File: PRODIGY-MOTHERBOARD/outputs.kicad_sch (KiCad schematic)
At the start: 36 parts, among them J10 MOTOR, J11 CAN, J3 A_IN, J4 SPI_OUT, J5 12V OUT, J6 I2C, J7 Neopixel, J8 USB_A, J9 SERIAL, U3 PCA9306DC

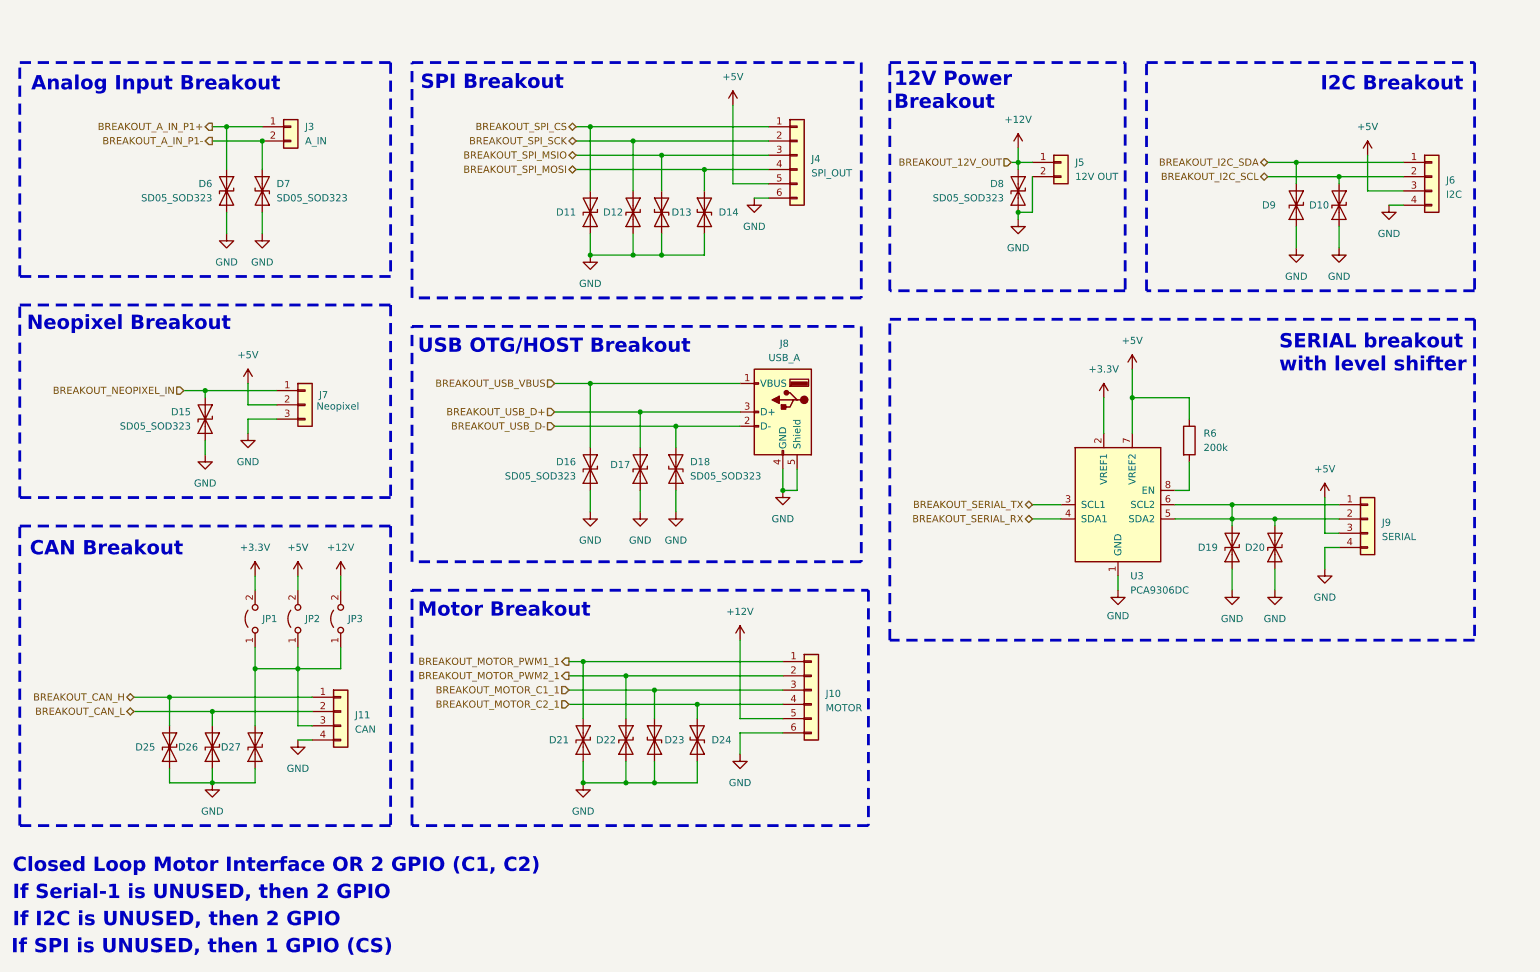
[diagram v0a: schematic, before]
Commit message: MCU schematic done. Started Analog design.
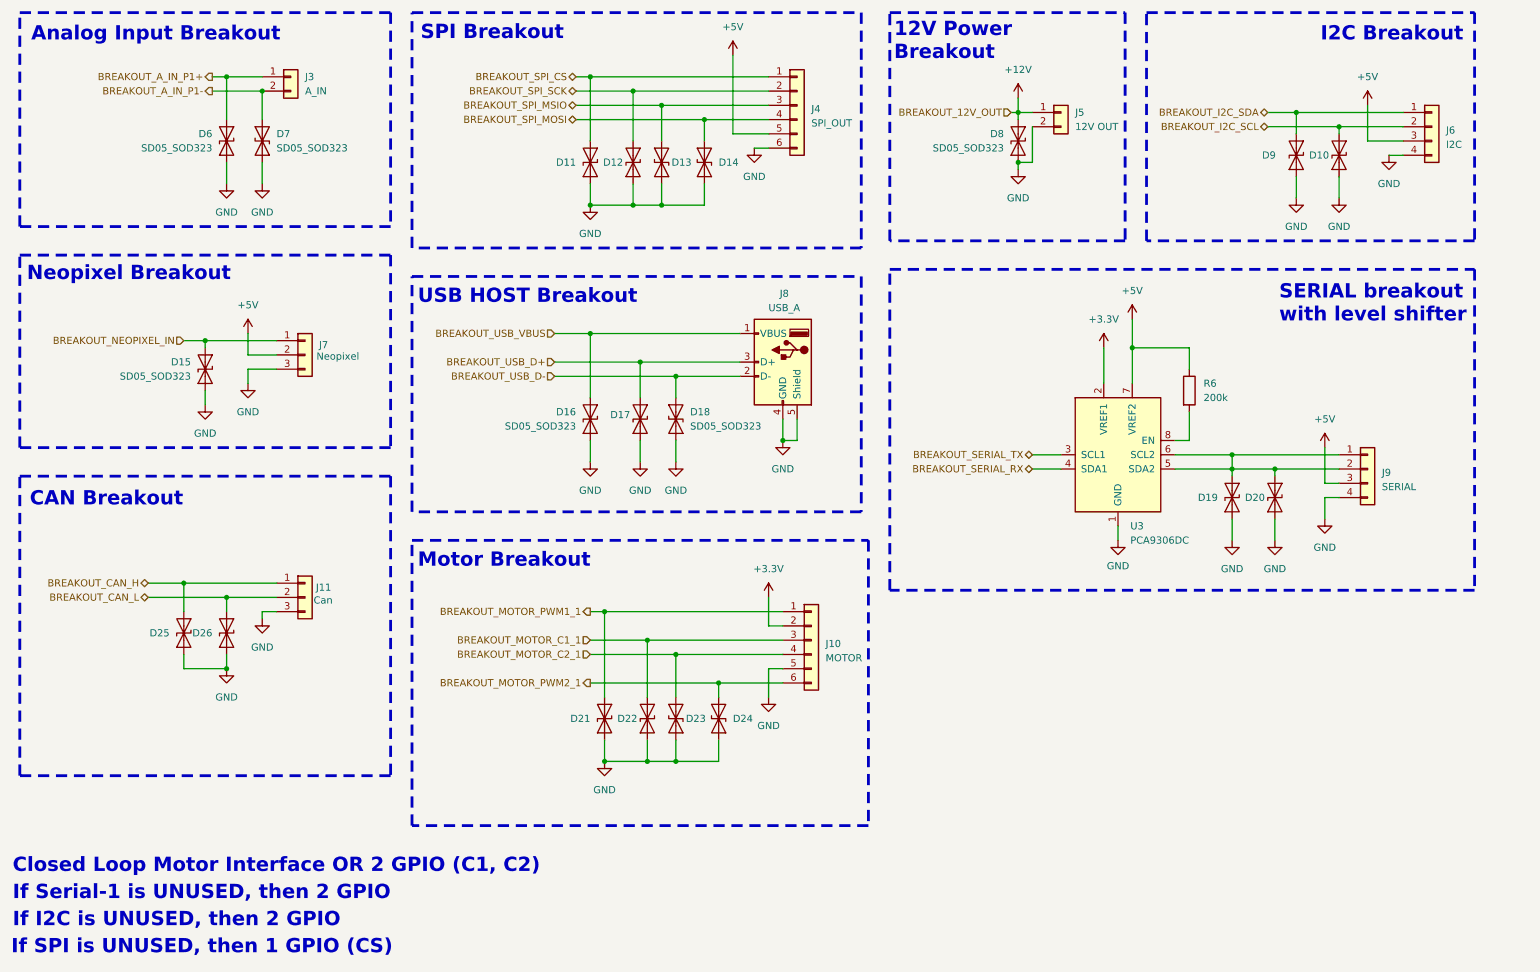
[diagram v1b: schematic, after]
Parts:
- removed D27: SD05_SOD323, Diode_SMD:D_SOD-323, symbol Diode:SD05_SOD323
- removed J11: CAN, Connector_JST:JST_XH_S4B-XH-A_1x04_P2.50mm_Horizontal, symbol Connector_Generic:Conn_01x04
- removed JP1, JP2, JP3: Jumper_2_Open, symbol Jumper:Jumper_2_Open
- added J11: Can, Connector_JST:JST_XH_S3B-XH-A_1x03_P2.50mm_Horizontal, symbol Connector_Generic:Conn_01x03
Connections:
- net +12V: no longer J10.5 (Pin_5)
- net +3.3V: now also J10.2 (Pin_2)
- net BREAKOUT_CAN_H: now also J11.1 (Pin_1)
- net BREAKOUT_CAN_L: now also J11.2 (Pin_2)
- net BREAKOUT_MOTOR_C1_1: now also D22.2 (A2); no longer D23.2 (A2)
- net BREAKOUT_MOTOR_C2_1: now also D23.2 (A2); no longer D24.2 (A2)
- net BREAKOUT_MOTOR_PWM2_1: now also D24.2 (A2), J10.6 (Pin_6); no longer D22.2 (A2), J10.2 (Pin_2)
- net GND: now also J10.5 (Pin_5), J11.3 (Pin_3); no longer J10.6 (Pin_6)
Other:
- note added: "USB HOST Breakout"
- note removed: "USB OTG/HOST Breakout"
- moved on the sheet: D10, D11, D12, D13, D14, D15, D16, D17, D18, D19, D20, D21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

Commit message: Finished v0.1 schematic.
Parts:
- added D30, D32, D33, D34: SD05_SOD323, Diode_SMD:D_SOD-323, symbol Diode:SD05_SOD323
- added J16: RTD_PT100, Connector_Phoenix_MSTB:PhoenixContact_MSTBA_2,5_4-G-5,08_1x04_P5.08mm_Horizontal, symbol Connector_Generic:Conn_01x04
- J10: renamed from J7; footprint Connector_JST:JST_XH_S3B-XH-A_1x03_P2.50mm_Horizontal -> Connector_Phoenix_MSTB:PhoenixContact_MSTBA_2,5_3-G-5,08_1x03_P5.08mm_Horizontal
- J11: footprint Connector_JST:JST_XH_S3B-XH-A_1x03_P2.50mm_Horizontal -> Connector_Phoenix_MSTB:PhoenixContact_MSTBA_2,5_3-G-5,08_1x03_P5.08mm_Horizontal
- J13: renamed from J4; footprint Connector_JST:JST_XH_S6B-XH-A_1x06_P2.50mm_Horizontal -> Connector_Phoenix_MSTB:PhoenixContact_MSTBA_2,5_6-G-5,08_1x06_P5.08mm_Horizontal
- J14: renamed from J10; footprint Connector_JST:JST_XH_S6B-XH-A_1x06_P2.50mm_Horizontal -> Connector_Phoenix_MSTB:PhoenixContact_MSTBA_2,5_6-G-5,08_1x06_P5.08mm_Horizontal
- J15: renamed from J5; footprint TerminalBlock_Phoenix:TerminalBlock_Phoenix_MKDS-1,5-2-5.08_1x02_P5.08mm_Horizontal -> Connector_Phoenix_MSTB:PhoenixContact_MSTBA_2,5_2-G-5,08_1x02_P5.08mm_Horizontal
- J17: renamed from J9; footprint Connector_JST:JST_XH_S4B-XH-A_1x04_P2.50mm_Horizontal -> Connector_Phoenix_MSTB:PhoenixContact_MSTBA_2,5_4-G-5,08_1x04_P5.08mm_Horizontal
- J18: renamed from J6; footprint Connector_JST:JST_XH_S4B-XH-A_1x04_P2.50mm_Horizontal -> Connector_Phoenix_MSTB:PhoenixContact_MSTBA_2,5_4-G-5,08_1x04_P5.08mm_Horizontal
- J9: renamed from J3; footprint Connector_JST:JST_XH_S3B-XH-A_1x02_P2.50mm_Horizontal -> Connector_Phoenix_MSTB:PhoenixContact_MSTBA_2,5_2-G-5,08_1x02_P5.08mm_Horizontal
- renumbered D25 to D14, D6 to D16, D26 to D17, D7 to D18, D11 to D19, D16 to D20, D12 to D22, D17 to D23, D22 to D24, D13 to D25, D18 to D26, D23 to D27, D14 to D28, D24 to D29, D8 to D31, D19 to D35, D20 to D36, D9 to D37, D10 to D38, J8 to J12, R6 to R26, U3 to U6
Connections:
- net GND: now also D30.1 (A1), D32.1 (A1), D33.1 (A1), D34.1 (A1)
- new net RTD_W1: D30.2 (A2), J16.1 (Pin_1)
- new net RTD_W2: D32.2 (A2), J16.2 (Pin_2)
- new net RTD_W3: D33.2 (A2), J16.3 (Pin_3)
- new net RTD_W4: D34.2 (A2), J16.4 (Pin_4)
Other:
- note added: "PT100/PT1000 Breakout"
- note added: "Piezo Sensor Input Breakout"
- note removed: "Analog Input Breakout"
- note removed: "Closed Loop Motor Interface OR 2 GPIO (C1, C2)"
- note removed: "If I2C is UNUSED, then 2 GPIO"
- note removed: "If SPI is UNUSED, then 1 GPIO (CS)"
- note removed: "If Serial-1 is UNUSED, then 2 GPIO"
- moved on the sheet: D14, D15, D17, J10, J11

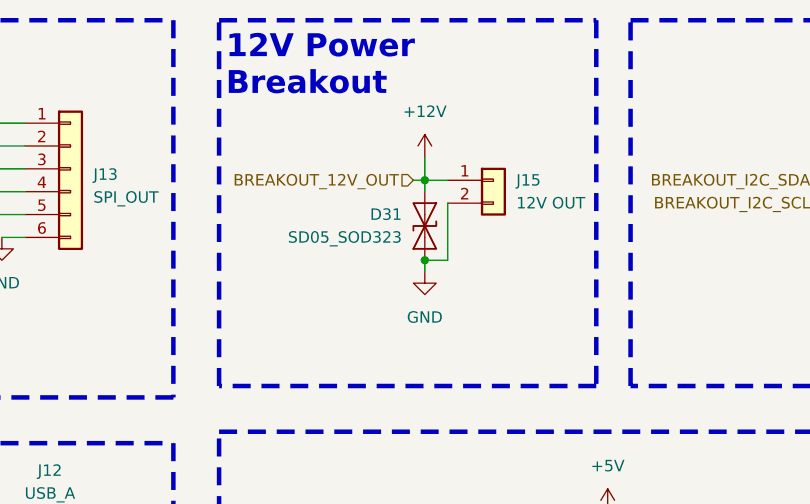
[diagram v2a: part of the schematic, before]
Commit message: MBT Schematic improved
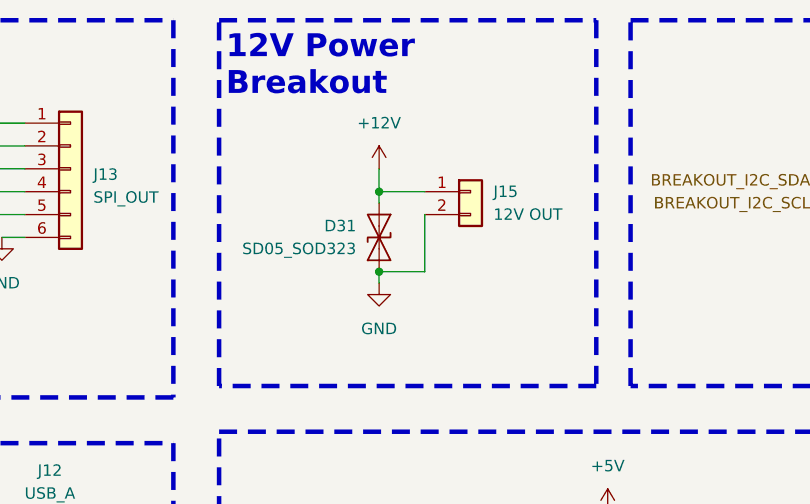
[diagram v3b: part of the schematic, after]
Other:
- moved on the sheet: D31, J15
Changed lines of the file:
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@@
 	(paper "A4")
 	(junction
-		(at 195.58 35.56)
+		(at 190.5 36.83)
 		(diameter 0)
 		(color 0 0 0 0)
@@
 	)
 	(junction
-		(at 195.58 44.45)
+		(at 190.5 45.72)
 		(diameter 0)
 		(color 0 0 0 0)
@@
 	(wire
 		(pts
-			(xy 195.58 33.02) (xy 195.58 35.56)
+			(xy 190.5 34.29) (xy 190.5 36.83)
 		)
 		(stroke
@@
 	(wire
 		(pts
-			(xy 195.58 36.83) (xy 195.58 35.56)
+			(xy 190.5 38.1) (xy 190.5 36.83)
 		)
 		(stroke
@@
 	(wire
 		(pts
-			(xy 195.58 35.56) (xy 198.12 35.56)
+			(xy 190.5 36.83) (xy 195.58 36.83)
 		)
 		(stroke
@@
 	(wire
 		(pts
-			(xy 194.31 35.56) (xy 195.58 35.56)
-		)
-		(stroke
-			(width 0)
-			(type default)
-		)
-	)
-	(wire
-		(pts
 			(xy 257.81 34.29) (xy 257.81 40.64)
 		)
@@
 	(wire
 		(pts
-			(xy 198.12 38.1) (xy 198.12 44.45)
+			(xy 195.58 39.37) (xy 195.58 45.72)
 		)
 		(stroke
@@
 	(wire
 		(pts
-			(xy 195.58 44.45) (xy 195.58 45.72)
+			(xy 190.5 45.72) (xy 190.5 46.99)
 		)
 		(stroke
@@
 	(wire
 		(pts
-			(xy 198.12 44.45) (xy 195.58 44.45)
+			(xy 195.58 45.72) (xy 190.5 45.72)
 		)
 		(stroke
@@
 		)
 	)
-	(hierarchical_label "BREAKOUT_12V_OUT"
-		(shape input)
-		(at 194.31 35.56 180)
-		(fields_autoplaced yes)
-		(effects
-			(font
-				(size 1.27 1.27)
-			)
-			(justify right)
-		)
-	)
 	(hierarchical_label "BREAKOUT_I2C_SDA"
 		(shape bidirectional)
@@
 	(symbol
 		(lib_id "power:GND")
-		(at 195.58 45.72 0)
+		(at 190.5 46.99 0)
 		(unit 1)
 		(exclude_from_sim no)
@@
 		(fields_autoplaced yes)
 		(property "Reference" "#PWR088"
-			(at 195.58 52.07 0)
+			(at 190.5 53.34 0)
 			(effects
 				(font
@@
 		)
 		(property "Value" "GND"
-			(at 195.58 50.8 0)
+			(at 190.5 52.07 0)
 			(effects
 				(font
@@
 		)
 		(property "Footprint" ""
-			(at 195.58 45.72 0)
+			(at 190.5 46.99 0)
 			(effects
 				(font
@@
 		)
 		(property "Datasheet" ""
-			(at 195.58 45.72 0)
+			(at 190.5 46.99 0)
 			(effects
 				(font
@@
 		)
 		(property "Description" ""
-			(at 195.58 45.72 0)
+			(at 190.5 46.99 0)
 			(effects
 				(font
@@
 	(symbol
 		(lib_id "Connector_Generic:Conn_01x02")
-		(at 203.2 35.56 0)
+		(at 200.66 36.83 0)
 		(unit 1)
 		(exclude_from_sim no)
@@
 		(fields_autoplaced yes)
 		(property "Reference" "J15"
-			(at 205.74 35.5599 0)
+			(at 203.2 36.8299 0)
 			(effects
 				(font
@@
 		)
 		(property "Value" "12V OUT "
-			(at 205.74 38.0999 0)
+			(at 203.2 39.3699 0)
 			(effects
 				(font
@@
 		)
 		(property "Footprint" "Connector_Phoenix_MSTB:PhoenixContact_MSTBA_2,5_2-G-5,08_1x02_P5.08mm_Horizontal"
-			(at 203.2 35.56 0)
+			(at 200.66 36.83 0)
 			(effects
 				(font
@@
 		)
 		(property "Datasheet" "~"
-			(at 203.2 35.56 0)
+			(at 200.66 36.83 0)
 			(effects
 				(font
@@
 		)
 		(property "Description" "Generic connector, single row, 01x02, script generated (kicad-library-utils/schlib/autogen/connector/)"
-			(at 203.2 35.56 0)
+			(at 200.66 36.83 0)
 			(effects
 				(font
@@
 	(symbol
 		(lib_id "power:+12V")
-		(at 195.58 33.02 0)
+		(at 190.5 34.29 0)
 		(unit 1)
 		(exclude_from_sim no)
@@
 		(fields_autoplaced yes)
 		(property "Reference" "#PWR087"
-			(at 195.58 36.83 0)
+			(at 190.5 38.1 0)
 			(effects
 				(font
@@
 		)
 		(property "Value" "+12V"
-			(at 195.58 27.94 0)
+			(at 190.5 29.21 0)
 			(effects
 				(font
@@
 		)
 		(property "Footprint" ""
-			(at 195.58 33.02 0)
+			(at 190.5 34.29 0)
 			(effects
 				(font
@@
 		)
 		(property "Datasheet" ""
-			(at 195.58 33.02 0)
+			(at 190.5 34.29 0)
 			(effects
 				(font
@@
 		)
 		(property "Description" "Power symbol creates a global label with name \"+12V\""
-			(at 195.58 33.02 0)
+			(at 190.5 34.29 0)
 			(effects
 				(font
@@
 	(symbol
 		(lib_id "Diode:SD05_SOD323")
-		(at 195.58 40.64 270)
+		(at 190.5 41.91 270)
 		(mirror x)
 		(unit 1)
@@
 		(dnp no)
 		(property "Reference" "D31"
-			(at 193.04 39.3699 90)
+			(at 187.96 40.6399 90)
 			(effects
 				(font
@@
 		)
 		(property "Value" "SD05_SOD323"
-			(at 193.04 41.9099 90)
+			(at 187.96 43.1799 90)
 			(effects
 				(font
@@
 		)
 		(property "Footprint" "Diode_SMD:D_SOD-323"
-			(at 190.5 40.64 0)
+			(at 185.42 41.91 0)
 			(effects
 				(font
@@
 		)
 		(property "Datasheet" "https://www.littelfuse.com/~/media/electronics/datasheets/tvs_diode_arrays/littelfuse_tvs_diode_array_sd_c_datasheet.pdf.pdf"
-			(at 195.58 40.64 0)
+			(at 190.5 41.91 0)
 			(effects
 				(font
@@
 		)
 		(property "Description" "5V, 450W Discrete Bidirectional TVS Diode, SOD-323"
-			(at 195.58 40.64 0)
+			(at 190.5 41.91 0)
 			(effects
 				(font

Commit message: schematic v0.2 finalized
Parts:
- renumbered D30 to D14, D32 to D15, D14 to D16, D33 to D17, D16 to D18, D17 to D19, D34 to D20, D18 to D21, D19 to D22, D20 to D23, D21 to D24, D22 to D25, D23 to D26, D24 to D27, D25 to D28, D26 to D29, D27 to D30, D28 to D31, D29 to D32, D31 to D33, D15 to D34, J16 to J10, J10 to J16

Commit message: changed breakout connectors and bpc size
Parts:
- J10, J17, J18: footprint Connector_Phoenix_MSTB:PhoenixContact_MSTBA_2,5_4-G-5,08_1x04_P5.08mm_Horizontal -> TerminalBlock_Phoenix:TerminalBlock_Phoenix_MKDS-1,5-4-5.08_1x04_P5.08mm_Horizontal
- J11, J16: footprint Connector_Phoenix_MSTB:PhoenixContact_MSTBA_2,5_3-G-5,08_1x03_P5.08mm_Horizontal -> TerminalBlock_Phoenix:TerminalBlock_Phoenix_MKDS-1,5-3-5.08_1x03_P5.08mm_Horizontal
- J13, J14: footprint Connector_Phoenix_MSTB:PhoenixContact_MSTBA_2,5_6-G-5,08_1x06_P5.08mm_Horizontal -> TerminalBlock_Phoenix:TerminalBlock_Phoenix_MKDS-1,5-6-5.08_1x06_P5.08mm_Horizontal
- J15, J9: footprint Connector_Phoenix_MSTB:PhoenixContact_MSTBA_2,5_2-G-5,08_1x02_P5.08mm_Horizontal -> TerminalBlock_Phoenix:TerminalBlock_Phoenix_MKDS-1,5-2-5.08_1x02_P5.08mm_Horizontal
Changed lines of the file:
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@@
 			)
 		)
-		(property "Footprint" "Connector_Phoenix_MSTB:PhoenixContact_MSTBA_2,5_6-G-5,08_1x06_P5.08mm_Horizontal"
+		(property "Footprint" "TerminalBlock_Phoenix:TerminalBlock_Phoenix_MKDS-1,5-6-5.08_1x06_P5.08mm_Horizontal"
 			(at 158.75 129.54 0)
 			(effects
@@
 			)
 		)
-		(property "Footprint" "Connector_Phoenix_MSTB:PhoenixContact_MSTBA_2,5_4-G-5,08_1x04_P5.08mm_Horizontal"
+		(property "Footprint" "TerminalBlock_Phoenix:TerminalBlock_Phoenix_MKDS-1,5-4-5.08_1x04_P5.08mm_Horizontal"
 			(at 269.24 38.1 0)
 			(effects
@@
 			)
 		)
-		(property "Footprint" "Connector_Phoenix_MSTB:PhoenixContact_MSTBA_2,5_4-G-5,08_1x04_P5.08mm_Horizontal"
+		(property "Footprint" "TerminalBlock_Phoenix:TerminalBlock_Phoenix_MKDS-1,5-4-5.08_1x04_P5.08mm_Horizontal"
 			(at 67.31 71.12 0)
 			(effects
@@
 			)
 		)
-		(property "Footprint" "Connector_Phoenix_MSTB:PhoenixContact_MSTBA_2,5_2-G-5,08_1x02_P5.08mm_Horizontal"
+		(property "Footprint" "TerminalBlock_Phoenix:TerminalBlock_Phoenix_MKDS-1,5-2-5.08_1x02_P5.08mm_Horizontal"
 			(at 200.66 36.83 0)
 			(effects
@@
 			)
 		)
-		(property "Footprint" "Connector_Phoenix_MSTB:PhoenixContact_MSTBA_2,5_3-G-5,08_1x03_P5.08mm_Horizontal"
+		(property "Footprint" "TerminalBlock_Phoenix:TerminalBlock_Phoenix_MKDS-1,5-3-5.08_1x03_P5.08mm_Horizontal"
 			(at 71.12 123.19 0)
 			(effects
@@
 			)
 		)
-		(property "Footprint" "Connector_Phoenix_MSTB:PhoenixContact_MSTBA_2,5_2-G-5,08_1x02_P5.08mm_Horizontal"
+		(property "Footprint" "TerminalBlock_Phoenix:TerminalBlock_Phoenix_MKDS-1,5-2-5.08_1x02_P5.08mm_Horizontal"
 			(at 66.04 29.21 0)
 			(effects
@@
 			)
 		)
-		(property "Footprint" "Connector_Phoenix_MSTB:PhoenixContact_MSTBA_2,5_6-G-5,08_1x06_P5.08mm_Horizontal"
+		(property "Footprint" "TerminalBlock_Phoenix:TerminalBlock_Phoenix_MKDS-1,5-6-5.08_1x06_P5.08mm_Horizontal"
 			(at 156.21 34.29 0)
 			(effects
@@
 			)
 		)
-		(property "Footprint" "Connector_Phoenix_MSTB:PhoenixContact_MSTBA_2,5_3-G-5,08_1x03_P5.08mm_Horizontal"
+		(property "Footprint" "TerminalBlock_Phoenix:TerminalBlock_Phoenix_MKDS-1,5-3-5.08_1x03_P5.08mm_Horizontal"
 			(at 224.79 143.51 0)
 			(effects
@@
 			)
 		)
-		(property "Footprint" "Connector_Phoenix_MSTB:PhoenixContact_MSTBA_2,5_4-G-5,08_1x04_P5.08mm_Horizontal"
+		(property "Footprint" "TerminalBlock_Phoenix:TerminalBlock_Phoenix_MKDS-1,5-4-5.08_1x04_P5.08mm_Horizontal"
 			(at 257.81 99.06 0)
 			(effects

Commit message: Motherboard footprints assigned.
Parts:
- R26: footprint (none) -> Resistor_SMD:R_0603_1608Metric
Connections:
- net +5V: no longer J17.3 (Pin_3), J18.3 (Pin_3)
- net +3.3V renamed VCC
- net VCC: now also J17.3 (Pin_3), J18.3 (Pin_3)
